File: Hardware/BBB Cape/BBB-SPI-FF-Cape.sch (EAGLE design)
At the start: 8 parts

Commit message: Complete routing for cape
Also updated the schematic just calling out the ground connections
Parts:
- U$1, U$2, U$3: OC_NEWARK (none) -> unknown
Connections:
- net GND: now also U$1.GND@2, U$1.GND@3, U$1.GND@4, U$1.GND@5, U$1.GND@6, U$1.GND@7, U$1.GND@8
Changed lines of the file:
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@@
 </classes>
 <parts>
-<part name="U$1" library="adafruit" deviceset="BEAGLEBONE_OUTLINE" device=""/>
+<part name="U$1" library="adafruit" deviceset="BEAGLEBONE_OUTLINE" device="">
+<attribute name="MF" value=""/>
+<attribute name="MPN" value=""/>
+<attribute name="OC_NEWARK" value="unknown"/>
+</part>
 <part name="JP2-SPI1" library="con-amp-quick" deviceset="M08" device=""/>
 <part name="JP3-SPI1" library="con-amp-quick" deviceset="M08" device=""/>
@@
 <part name="GND3" library="supply1" deviceset="GND" device=""/>
 <part name="P+2" library="supply1" deviceset="VCC" device=""/>
-<part name="U$2" library="MADCAT-BBB-Cape" deviceset="CL-SB-23B-01T" device="SMD"/>
-<part name="U$3" library="MADCAT-BBB-Cape" deviceset="CL-SB-23B-01T" device="SMD"/>
+<part name="U$2" library="MADCAT-BBB-Cape" deviceset="CL-SB-23B-01T" device="SMD">
+<attribute name="MF" value=""/>
+<attribute name="MPN" value=""/>
+<attribute name="OC_NEWARK" value="unknown"/>
+</part>
+<part name="U$3" library="MADCAT-BBB-Cape" deviceset="CL-SB-23B-01T" device="SMD">
+<attribute name="MF" value=""/>
+<attribute name="MPN" value=""/>
+<attribute name="OC_NEWARK" value="unknown"/>
+</part>
 </parts>
 <sheets>
@@
 </plain>
 <instances>
-<instance part="U$1" gate="G$1" x="-10.16" y="58.42"/>
+<instance part="U$1" gate="G$1" x="-10.16" y="58.42">
+<attribute name="OC_NEWARK" x="-10.16" y="58.42" size="1.778" layer="96" display="off"/>
+<attribute name="MF" x="-10.16" y="58.42" size="1.778" layer="96" display="off"/>
+<attribute name="MPN" x="-10.16" y="58.42" size="1.778" layer="96" display="off"/>
+</instance>
 <instance part="JP2-SPI1" gate="G$1" x="101.6" y="106.68" rot="MR0"/>
 <instance part="JP3-SPI1" gate="G$1" x="101.6" y="66.04" rot="MR0"/>
@@
 <instance part="GND3" gate="1" x="109.22" y="0"/>
 <instance part="P+2" gate="VCC" x="114.3" y="0" rot="R180"/>
-<instance part="U$2" gate="G$1" x="50.8" y="106.68" rot="R270"/>
-<instance part="U$3" gate="G$1" x="50.8" y="66.04" rot="R90"/>
+<instance part="U$2" gate="G$1" x="50.8" y="106.68" rot="R270">
+<attribute name="OC_NEWARK" x="50.8" y="106.68" size="1.778" layer="96" display="off"/>
+<attribute name="MF" x="50.8" y="106.68" size="1.778" layer="96" display="off"/>
+<attribute name="MPN" x="50.8" y="106.68" size="1.778" layer="96" display="off"/>
+</instance>
+<instance part="U$3" gate="G$1" x="50.8" y="66.04" rot="R90">
+<attribute name="OC_NEWARK" x="50.8" y="66.04" size="1.778" layer="96" display="off"/>
+<attribute name="MF" x="50.8" y="66.04" size="1.778" layer="96" display="off"/>
+<attribute name="MPN" x="50.8" y="66.04" size="1.778" layer="96" display="off"/>
+</instance>
 </instances>
 <busses>
@@
 <wire x1="109.22" y1="10.16" x2="109.22" y2="2.54" width="0.1524" layer="91"/>
 </segment>
+<segment>
+<pinref part="U$1" gate="G$1" pin="GND@7"/>
+<wire x1="-38.1" y1="119.38" x2="-48.26" y2="119.38" width="0.1524" layer="91"/>
+<label x="-48.26" y="119.38" size="1.778" layer="95"/>
+</segment>
+<segment>
+<pinref part="U$1" gate="G$1" pin="GND@8"/>
+<wire x1="17.78" y1="119.38" x2="27.94" y2="119.38" width="0.1524" layer="91"/>
+<label x="22.86" y="119.38" size="1.778" layer="95"/>
+</segment>
+<segment>
+<pinref part="U$1" gate="G$1" pin="GND@2"/>
+<wire x1="17.78" y1="53.34" x2="27.94" y2="53.34" width="0.1524" layer="91"/>
+<label x="22.86" y="53.34" size="1.778" layer="95"/>
+</segment>
+<segment>
+<pinref part="U$1" gate="G$1" pin="GND@3"/>
+<wire x1="-38.1" y1="0" x2="-48.26" y2="0" width="0.1524" layer="91"/>
+<label x="-48.26" y="0" size="1.778" layer="95"/>
+</segment>
+<segment>
+<pinref part="U$1" gate="G$1" pin="GND@4"/>
+<wire x1="-38.1" y1="-2.54" x2="-48.26" y2="-2.54" width="0.1524" layer="91"/>
+<label x="-48.26" y="-2.54" size="1.778" layer="95"/>
+</segment>
+<segment>
+<pinref part="U$1" gate="G$1" pin="GND@5"/>
+<wire x1="17.78" y1="0" x2="27.94" y2="0" width="0.1524" layer="91"/>
+<label x="22.86" y="0" size="1.778" layer="95"/>
+</segment>
+<segment>
+<pinref part="U$1" gate="G$1" pin="GND@6"/>
+<wire x1="17.78" y1="-2.54" x2="27.94" y2="-2.54" width="0.1524" layer="91"/>
+<label x="22.86" y="-2.54" size="1.778" layer="95"/>
+</segment>
 </net>

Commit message: Updated switch lay out and routing
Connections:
- new net FF-CLK: JP2-SPI1.7, U$2.P$7
- net CS: now also U$2.P$5; no longer JP2-SPI1.7, U$2.P$7
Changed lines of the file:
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@@
 <net name="CS" class="0">
-<segment>
-<pinref part="JP2-SPI1" gate="G$1" pin="7"/>
-<label x="91.44" y="114.3" size="1.778" layer="95"/>
-<wire x1="96.52" y1="114.3" x2="86.36" y2="114.3" width="0.1524" layer="91"/>
-<pinref part="U$2" gate="G$1" pin="P$7"/>
-<wire x1="86.36" y1="114.3" x2="86.36" y2="101.6" width="0.1524" layer="91"/>
-<wire x1="86.36" y1="101.6" x2="60.96" y2="101.6" width="0.1524" layer="91"/>
-</segment>
 <segment>
 <pinref part="U$1" gate="G$1" pin="I2C1_SCL"/>
 <wire x1="-38.1" y1="33.02" x2="-48.26" y2="33.02" width="0.1524" layer="91"/>
 <label x="-48.26" y="33.02" size="1.778" layer="95"/>
+</segment>
+<segment>
+<pinref part="U$2" gate="G$1" pin="P$5"/>
+<wire x1="60.96" y1="114.3" x2="66.04" y2="114.3" width="0.1524" layer="91"/>
+<label x="60.96" y="114.3" size="1.778" layer="95"/>
 </segment>
 </net>
@@
 </segment>
 </net>
+<net name="FF-CLK" class="0">
+<segment>
+<pinref part="JP2-SPI1" gate="G$1" pin="7"/>
+<label x="88.9" y="114.3" size="1.778" layer="95"/>
+<pinref part="U$2" gate="G$1" pin="P$7"/>
+<wire x1="60.96" y1="101.6" x2="86.36" y2="101.6" width="0.1524" layer="91"/>
+<wire x1="86.36" y1="101.6" x2="86.36" y2="114.3" width="0.1524" layer="91"/>
+<wire x1="86.36" y1="114.3" x2="96.52" y2="114.3" width="0.1524" layer="91"/>
+</segment>
+</net>

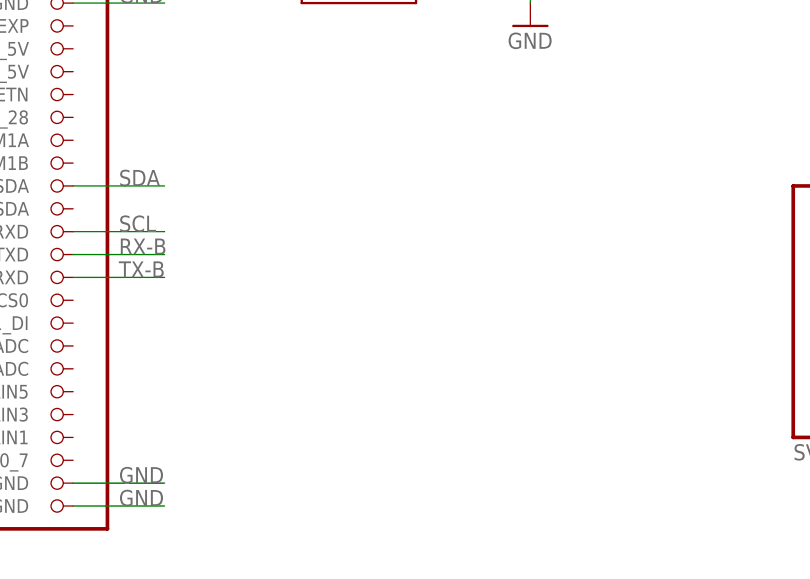
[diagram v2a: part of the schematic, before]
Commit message: Added Indicator LED
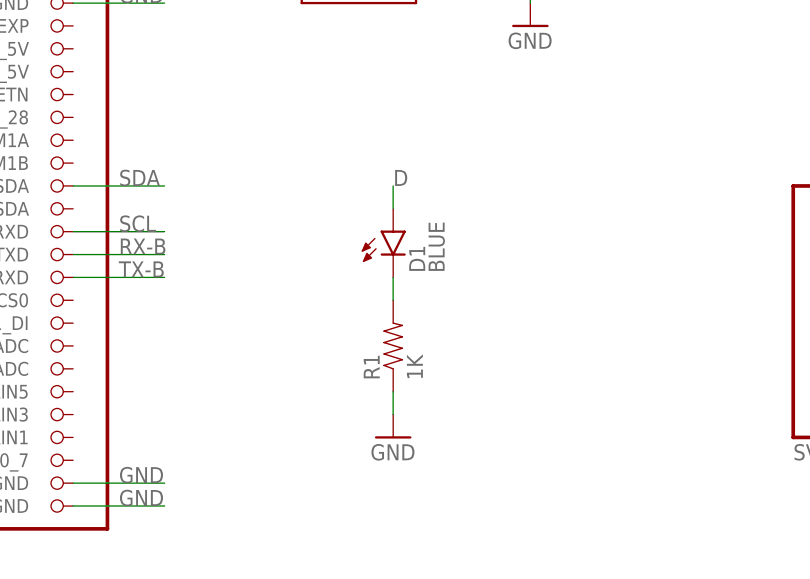
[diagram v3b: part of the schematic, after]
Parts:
- added D1: BLUE, SparkFun-LED:LED-BLUE1206
- added R1: 1K, SparkFun-Resistors:1KOHM-1/10W-1%(0603)
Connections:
- new net N$1: D1.C, R1.2
- net D: now also D1.A
- net GND: now also R1.1
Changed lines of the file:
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@@
 <attribute name="OC_NEWARK" value="unknown"/>
 </part>
+<part name="D1" library="SparkFun-LED" deviceset="LED-BLUE" device="1206" value="BLUE"/>
+<part name="R1" library="SparkFun-Resistors" deviceset="1KOHM-1/10W-1%(0603)" device="" value="1K"/>
+<part name="GND4" library="SparkFun-Aesthetics" deviceset="GND" device=""/>
 </parts>
 <sheets>
@@
 <attribute name="MPN" x="50.8" y="66.04" size="1.778" layer="96" display="off"/>
 </instance>
+<instance part="D1" gate="G$1" x="53.34" y="27.94"/>
+<instance part="R1" gate="G$1" x="53.34" y="15.24" rot="R90"/>
+<instance part="GND4" gate="1" x="53.34" y="5.08"/>
 </instances>
 <busses>
@@
 <label x="22.86" y="-2.54" size="1.778" layer="95"/>
 </segment>
+<segment>
+<pinref part="R1" gate="G$1" pin="1"/>
+<pinref part="GND4" gate="1" pin="GND"/>
+<wire x1="53.34" y1="10.16" x2="53.34" y2="7.62" width="0.1524" layer="91"/>
+</segment>
 </net>
 <net name="VCC" class="0">
@@
 <label x="88.9" y="66.04" size="1.778" layer="95" rot="R90"/>
 </segment>
+<segment>
+<pinref part="D1" gate="G$1" pin="A"/>
+<wire x1="53.34" y1="30.48" x2="53.34" y2="33.02" width="0.1524" layer="91"/>
+<label x="53.34" y="33.02" size="1.778" layer="95"/>
+</segment>
 </net>
 <net name="CS" class="0">
@@
 </segment>
 </net>
+<net name="N$1" class="0">
+<segment>
+<pinref part="R1" gate="G$1" pin="2"/>
+<pinref part="D1" gate="G$1" pin="C"/>
+<wire x1="53.34" y1="22.86" x2="53.34" y2="20.32" width="0.1524" layer="91"/>
+</segment>
+</net>

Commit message: Fixed the headers for the M08 cables coming from the IMU
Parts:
- JP2-SPI1, JP2-SPIN, JP3-SPI1: device con-amp-quick:M08 -> SparkFun-Connectors:M08BM08B-SRSS-TB
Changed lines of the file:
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@@
 <layer number="112" name="tSilk" color="7" fill="1" visible="no" active="yes"/>
 <layer number="113" name="ReferenceLS" color="7" fill="1" visible="no" active="no"/>
+<layer number="114" name="Badge_Outline" color="7" fill="1" visible="yes" active="yes"/>
+<layer number="115" name="ReferenceISLANDS" color="7" fill="1" visible="yes" active="yes"/>
 <layer number="116" name="Patch_BOT" color="9" fill="4" visible="no" active="yes"/>
 <layer number="118" name="Rect_Pads" color="7" fill="1" visible="no" active="no"/>
@@
 <attribute name="OC_NEWARK" value="unknown"/>
 </part>
-<part name="JP2-SPI1" library="con-amp-quick" deviceset="M08" device=""/>
-<part name="JP3-SPI1" library="con-amp-quick" deviceset="M08" device=""/>
+<part name="JP2-SPI1" library="SparkFun-Connectors" deviceset="M08" device="BM08B-SRSS-TB"/>
+<part name="JP3-SPI1" library="SparkFun-Connectors" deviceset="M08" device="BM08B-SRSS-TB"/>
 <part name="GND1" library="supply1" deviceset="GND" device=""/>
 <part name="GND2" library="supply1" deviceset="GND" device=""/>
 <part name="P+4" library="supply1" deviceset="VCC" device=""/>
 <part name="P+6" library="supply1" deviceset="VCC" device=""/>
-<part name="JP2-SPIN" library="con-amp-quick" deviceset="M08" device=""/>
+<part name="JP2-SPIN" library="SparkFun-Connectors" deviceset="M08" device="BM08B-SRSS-TB"/>
 <part name="P+1" library="supply1" deviceset="VCC" device=""/>
 <part name="GND5" library="supply1" deviceset="GND" device=""/>

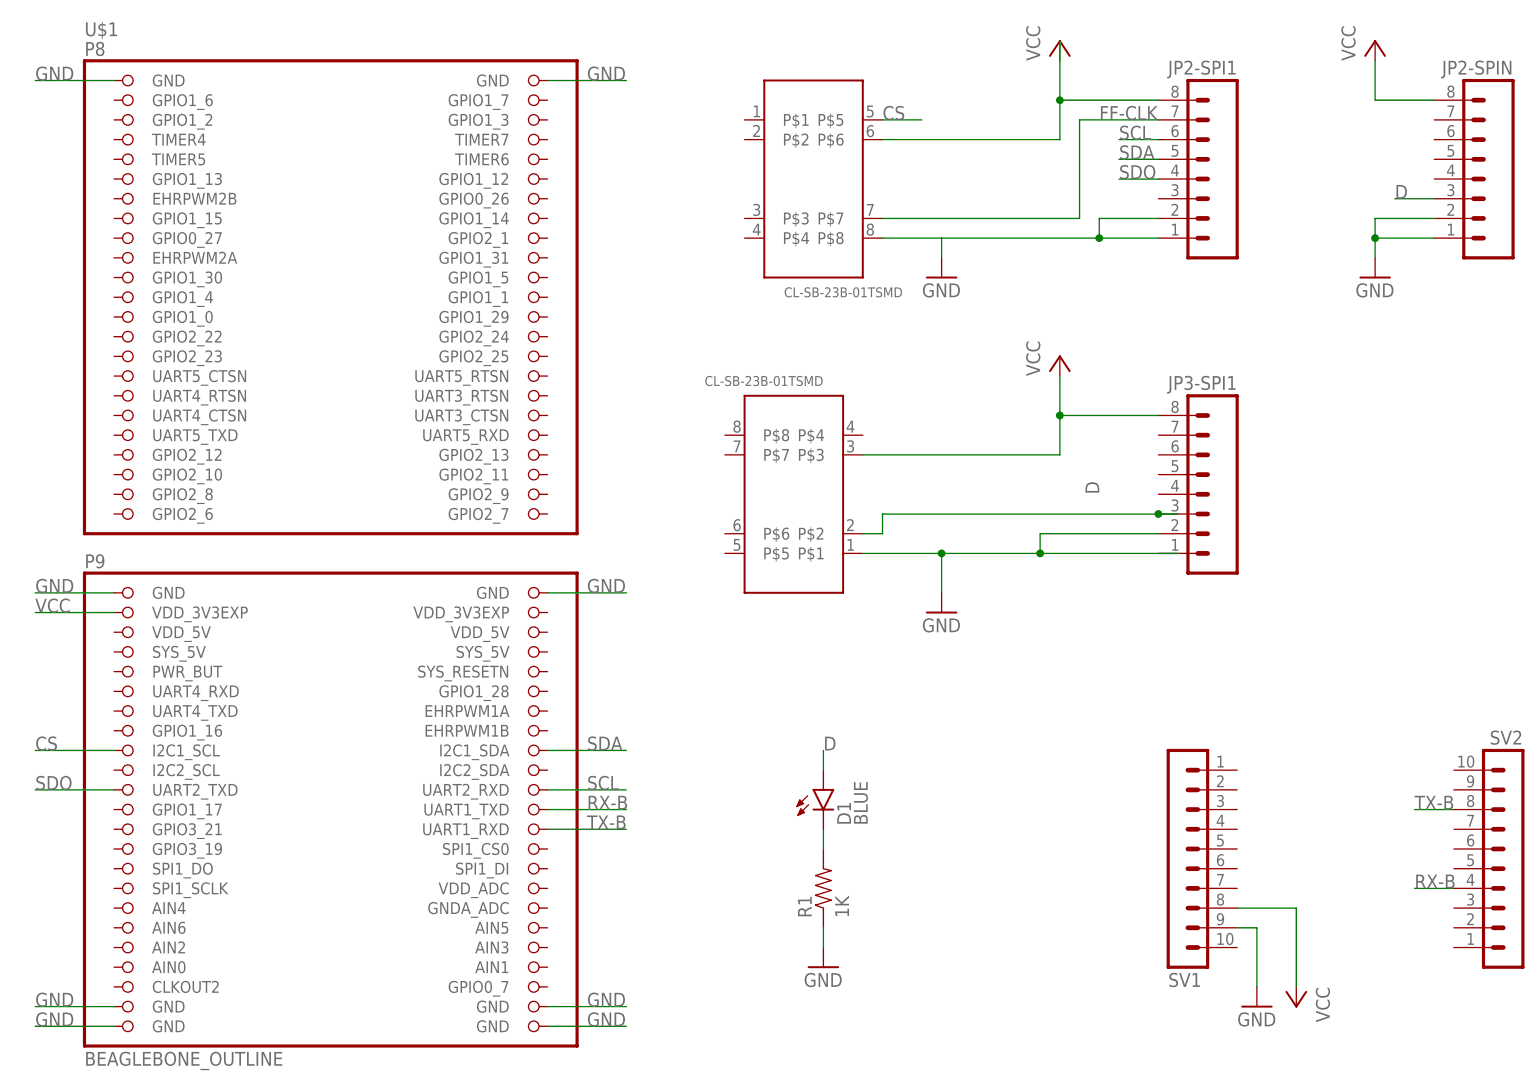
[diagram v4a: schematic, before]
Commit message: Split cape into two components
Lower layer is the GPS and Pot and upper layer is the SPI connections
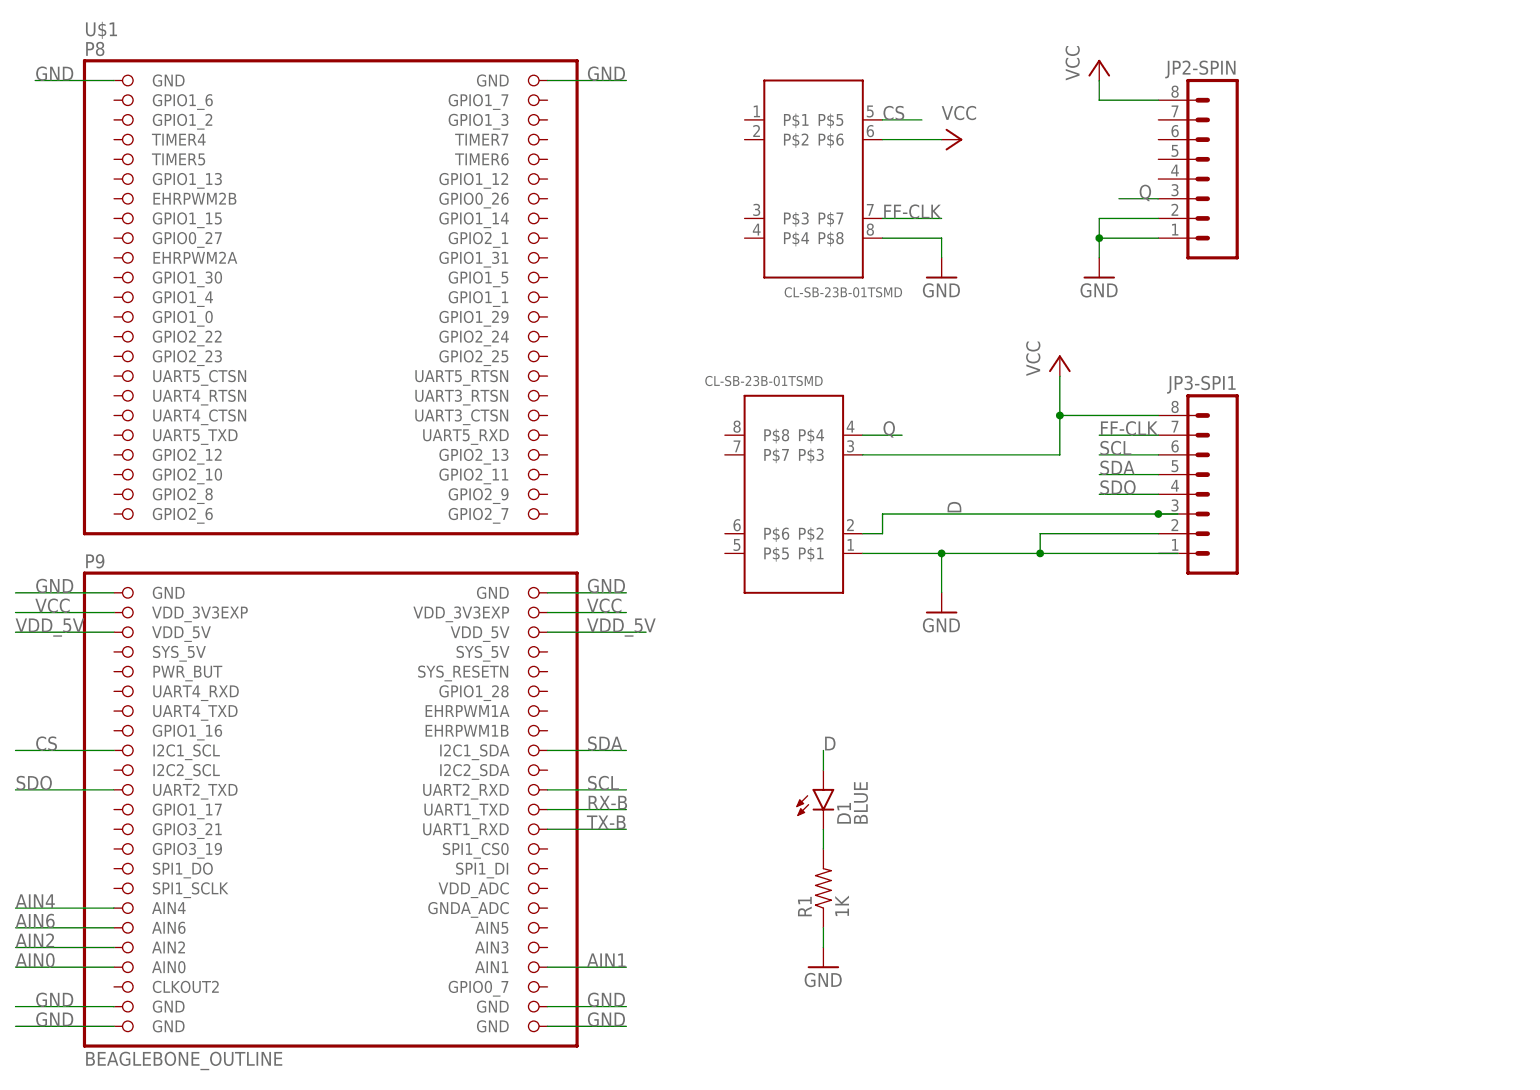
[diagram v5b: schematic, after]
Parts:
- removed JP2-SPI1: (no value), SparkFun-Connectors:M08BM08B-SRSS-TB
- removed SV1, SV2: (no value), con-lstb:MA10-1
- R1: device SparkFun-Resistors:1KOHM-1/10W-1%(0603) -> SparkFun-Resistors:RESISTOR1206
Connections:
- removed net N$3: JP2-SPI1.8, U$2.P$6
- new net AIN0: U$1.AIN0
- new net AIN1: U$1.AIN1
- new net AIN2: U$1.AIN2
- new net AIN4: U$1.AIN4
- new net AIN6: U$1.AIN6
- new net Q: JP2-SPIN.3, U$3.P$4
- new net VDD_5V: U$1.VDD_5V@1, U$1.VDD_5V@2
- net D: no longer JP2-SPIN.3
- net FF-CLK: now also JP3-SPI1.7; no longer JP2-SPI1.7
- net GND: no longer JP2-SPI1.1, JP2-SPI1.2, SV1.9
- net RX-B: no longer SV2.4
- net SCL: now also JP3-SPI1.6; no longer JP2-SPI1.6
- net SDA: now also JP3-SPI1.5; no longer JP2-SPI1.5
- net SDO: now also JP3-SPI1.4; no longer JP2-SPI1.4
- net TX-B: no longer SV2.8
- net VCC: now also U$1.VDD_3V3EXP@2, U$2.P$6; no longer SV1.8
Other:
- moved on the sheet: JP2-SPIN
